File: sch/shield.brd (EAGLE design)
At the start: 59.7 x 53.3 mm, 19 parts, among them IC1 LM1881

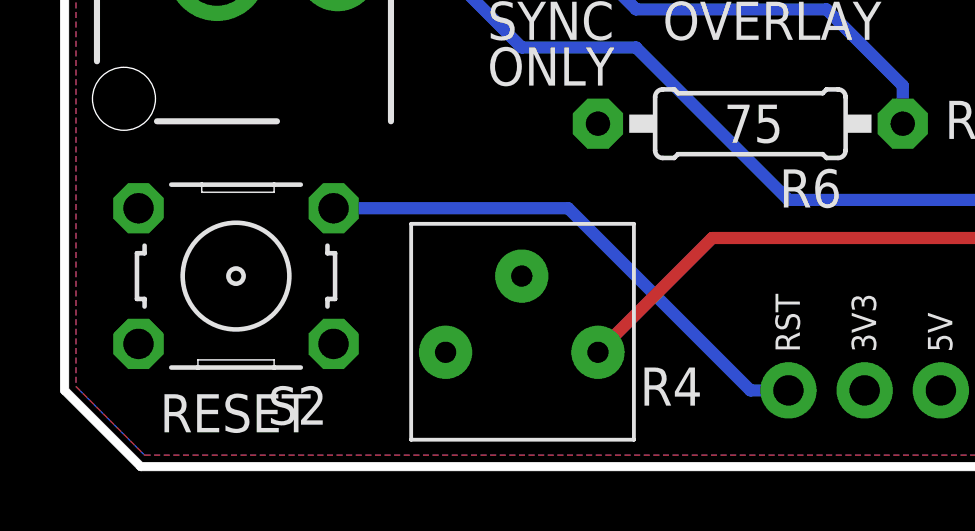
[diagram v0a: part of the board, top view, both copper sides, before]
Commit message: sch: Remove unneeded connections
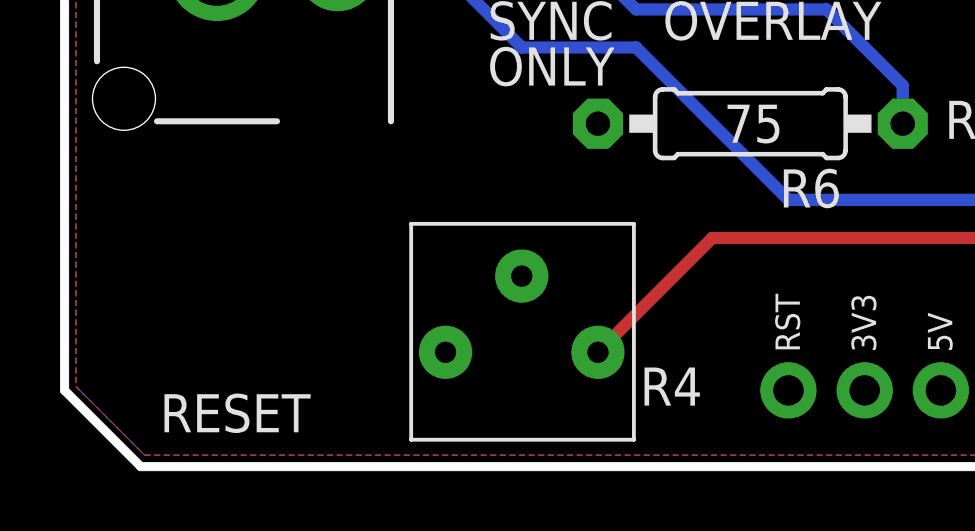
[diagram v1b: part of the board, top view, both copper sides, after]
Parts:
- removed S2: SWITCH-TACTSWITCH-TACT-B, nootropicdesign:SWITCH-TACT-B
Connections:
- removed net RESET: S2.3, U$2.RES
- net +5V: no longer U$2.5V
- net GND: no longer S2.1, U$2.GND@0, U$2.GND@1, U$2.GND@2
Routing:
- net RESET: track 17.7 -> 0.00 mm
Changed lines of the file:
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@@
 <element name="R6" library="nootropicdesign" package="0207/10" value="75" x="22.86" y="11.43" rot="R180"/>
 <element name="R5" library="nootropicdesign" package="0207/10" value="20K" x="27.94" y="43.18" rot="R180"/>
-<element name="S2" library="nootropicdesign" package="SWITCH-TACT-B" value="SWITCH-TACTSWITCH-TACT-B" x="5.715" y="6.35" rot="R180"/>
 <element name="U$5" library="nootropicdesign" package="TRIM_POT_TIGHT" value="TRIMPOTTIGHT" x="15.24" y="3.81" rot="R90"/>
 </elements>
@@
 <contactref element="OUTPUT" pad="BARREL"/>
 <contactref element="INPUT" pad="BARREL"/>
-<contactref element="U$2" pad="GND@2"/>
-<contactref element="U$2" pad="GND@1"/>
-<contactref element="U$2" pad="GND@0"/>
 <contactref element="IC1" pad="4"/>
 <contactref element="C3" pad="2"/>
@@
 </polygon>
 <contactref element="R6" pad="2"/>
-<contactref element="S2" pad="1"/>
 <contactref element="U$5" pad="2"/>
+<wire x1="43.18" y1="17.78" x2="54.61" y2="16.51" width="0" layer="19" extent="1-1"/>
+<wire x1="35.56" y1="17.78" x2="43.18" y2="17.78" width="0" layer="19" extent="1-1"/>
+<wire x1="33.02" y1="29.21" x2="35.56" y2="17.78" width="0" layer="19" extent="1-1"/>
+<wire x1="17.78" y1="11.43" x2="35.56" y2="17.78" width="0" layer="19" extent="1-1"/>
+<wire x1="15.24" y1="6.35" x2="17.78" y2="11.43" width="0" layer="19" extent="1-1"/>
+<wire x1="5.08" y1="16.51" x2="17.78" y2="11.43" width="0" layer="19" extent="1-1"/>
+<wire x1="10.16" y1="50.8" x2="33.02" y2="29.21" width="0" layer="19" extent="1-1"/>
 </signal>
 <signal name="N$3">
@@
 <wire x1="44.45" y1="8.89" x2="46.99" y2="6.35" width="0.4064" layer="1"/>
 <wire x1="46.99" y1="6.35" x2="46.99" y2="2.54" width="0.4064" layer="1"/>
-</signal>
-<signal name="RESET">
-<contactref element="U$2" pad="RES"/>
-<wire x1="16.7894" y1="8.6106" x2="22.86" y2="2.54" width="0.4064" layer="16"/>
-<wire x1="22.86" y1="2.54" x2="24.13" y2="2.54" width="0.4064" layer="16"/>
-<contactref element="S2" pad="3"/>
-<wire x1="8.9662" y1="8.6106" x2="16.7894" y2="8.6106" width="0.4064" layer="16"/>
 </signal>
 <signal name="N$29">
@@
 </polygon>
 <contactref element="R5" pad="1"/>
-<contactref element="U$2" pad="5V"/>
+<wire x1="40.64" y1="21.59" x2="33.02" y2="43.18" width="0" layer="19" extent="1-1"/>
+<wire x1="40.64" y1="17.78" x2="40.64" y2="21.59" width="0" layer="19" extent="1-1"/>
 </signal>
 <signal name="N$1">
